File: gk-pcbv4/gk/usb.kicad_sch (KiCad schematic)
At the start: 15 parts, among them J6 USB_A, J7 USB_C_Receptacle_USB2.0, U10 WE-TVS-82400102, U11 WE-TVS-82400102, U8 TPS2051CDBV, U9 TLV61070ADBV

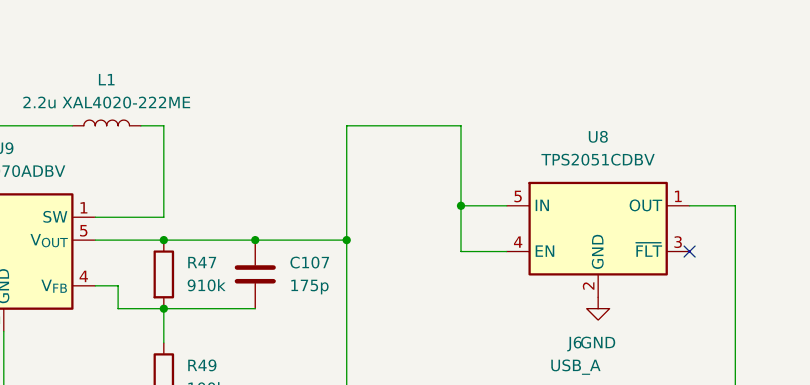
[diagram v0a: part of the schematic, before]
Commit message: add test points to power planes
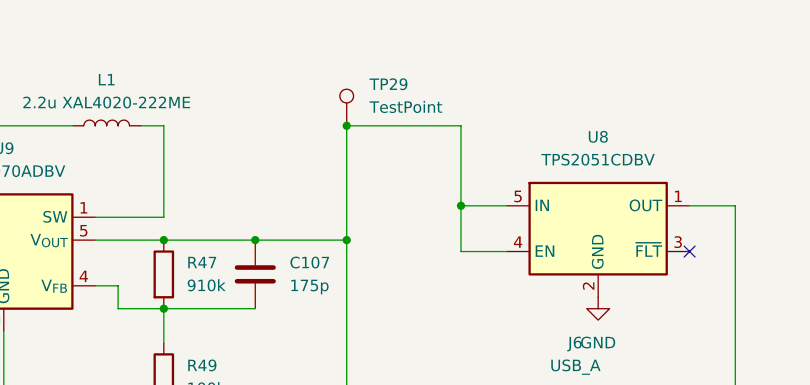
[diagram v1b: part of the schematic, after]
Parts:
- added TP29: TestPoint, TestPoint:TestPoint_Pad_D1.0mm, symbol Connector:TestPoint
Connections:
- net at C107.1, C108.1, R47.1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: now also TP29.1
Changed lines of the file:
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@@
+	)
+	(junction
+		(at 99.06 30.48)
+		(diameter 0)
+		(color 0 0 0 0)
 	)
 	(junction
@@
 					(unit 1)
 				)
+			)
+		)
+	)
+	(symbol
+		(lib_id "Connector:TestPoint")
+		(at 99.06 30.48 0)
+		(unit 1)
+		(exclude_from_sim no)
+		(in_bom yes)
+		(on_board yes)
+		(dnp no)
+		(fields_autoplaced yes)
+		(property "Reference" "TP29"
+			(at 101.6 25.9079 0)
+			(effects
+				(font
+					(size 1.27 1.27)
+				)
+				(justify left)
+			)
+		)
+		(property "Value" "TestPoint"
+			(at 101.6 28.4479 0)
+			(effects
+				(font
+					(size 1.27 1.27)
+				)
+				(justify left)
+			)
+		)
+		(property "Footprint" "TestPoint:TestPoint_Pad_D1.0mm"
+			(at 104.14 30.48 0)
+			(effects
+				(font
+					(size 1.27 1.27)
+				)
+				(hide yes)
+			)
+		)
+		(property "Datasheet" "~"
+			(at 104.14 30.48 0)
+			(effects
+				(font
+					(size 1.27 1.27)
+				)
+				(hide yes)
+			)
+		)
+		(property "Description" "test point"
+			(at 99.06 30.48 0)
+			(effects
+				(font
+					(size 1.27 1.27)
+				)
+				(hide yes)
+			)
+		)
+		(pin "1"
+		)
+		(instances
+			(project "gk"
+				(path "/a049c72e-5361-408c-ab21-661d491fee9d/c13f55c1-fb19-4613-ae88-39652b456244"
+					(reference "TP29")
+					(unit 1)
+				)
